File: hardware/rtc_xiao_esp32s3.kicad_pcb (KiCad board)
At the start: 4 copper layers, 17.5 x 21 mm, 24 parts, among them J1 +5V, J2 GND, J3 SCL, J4 SDA, J5 CLKOUT, J6 NINT, U1 RV-3028-C8

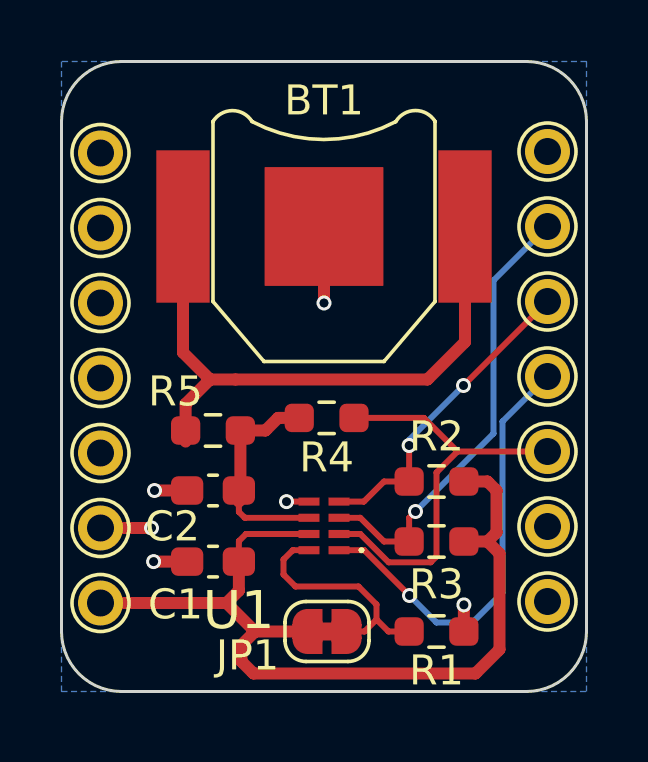
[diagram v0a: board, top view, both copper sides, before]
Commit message: pcb update - routing
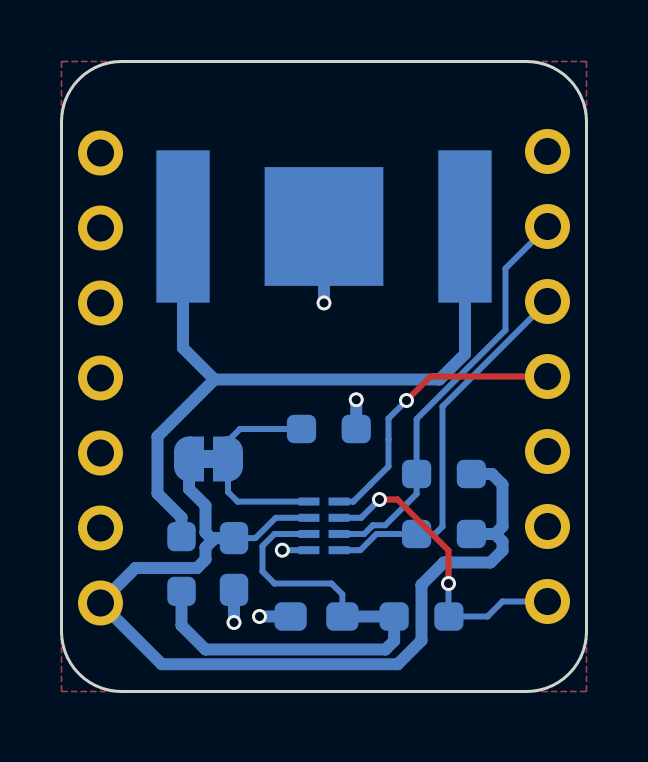
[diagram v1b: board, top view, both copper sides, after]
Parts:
- BT1, C1, C2, J1, J2 (x9), J3, J4, J5, J6, JP1, R1, R2, R3, R4, R5, U1: moved to B.Cu
- moved R1 7.64 mm to (124.9, 107.2)
- moved R4 7.34 mm to (128.0, 113.5)
- moved JP1 6.98 mm to (120.9, 108.2)
- moved C2 5.44 mm to (124.5, 113.5)
- moved J2 5.00 mm to (132.2, 108.0), turned to 180 degrees
- moved J6 5.00 mm to (132.2, 113.0), turned to 180 degrees
- moved R5 4.57 mm to (120.0, 111.8), turned to 90 degrees
- moved R3 2.26 mm to (128.8, 108.8)
- moved R2 1.77 mm to (128.8, 110.8)
- moved C1 0.70 mm to (121.8, 111.8), turned to 90 degrees
- turned BT1 to 180 degrees
- turned J1 to 180 degrees
- turned J2 to 180 degrees (x3)
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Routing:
- net /VBACKUP: track 7.36 -> 17.5 mm
- net CLKOUT: track 14.7 -> 9.61 mm
- net NINT: track 14.4 -> 10.3 mm, vias 0 -> 2
- net /batt_to_r: track 20.7 -> 24.8 mm
- net +5V: track 29.8 -> 33.3 mm
- net SDA: track 10.5 -> 12.7 mm, vias 2 -> 0
- net GND: track 8.09 -> 6.54 mm, vias 6 -> 5
- net SCL: track 15.1 -> 13.9 mm, vias 1 -> 0
- net /EVI: track 7.91 -> 7.15 mm
- added copper zone on F.Cu, net GND
